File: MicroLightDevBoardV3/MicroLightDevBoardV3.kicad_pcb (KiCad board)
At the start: 2 copper layers, 12.9 x 18.9 mm, 26 parts, among them J1 TYPE-C-31-M-12, J2 Conn_01x02_Socket, J3 Conn_01x03_Socket, SW1 SW_Push, U1 USBLC6-2P6, U2 STM32C071GBUx, U3 BQ25180, U4 S-85S1AB33-I6T1U

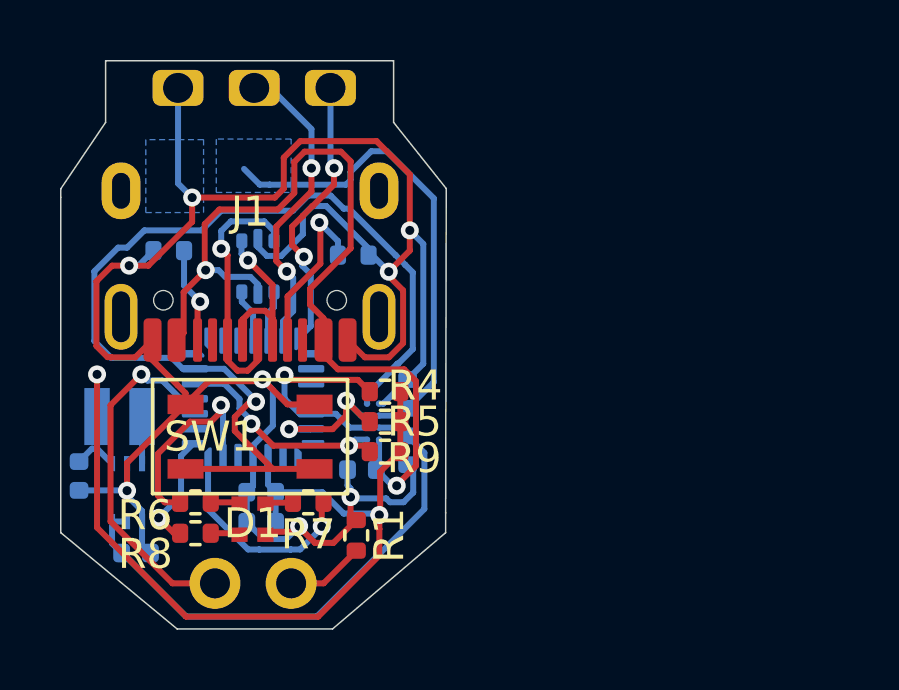
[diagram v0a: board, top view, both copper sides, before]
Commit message: change battery attachment from pad to through hole to increase durability
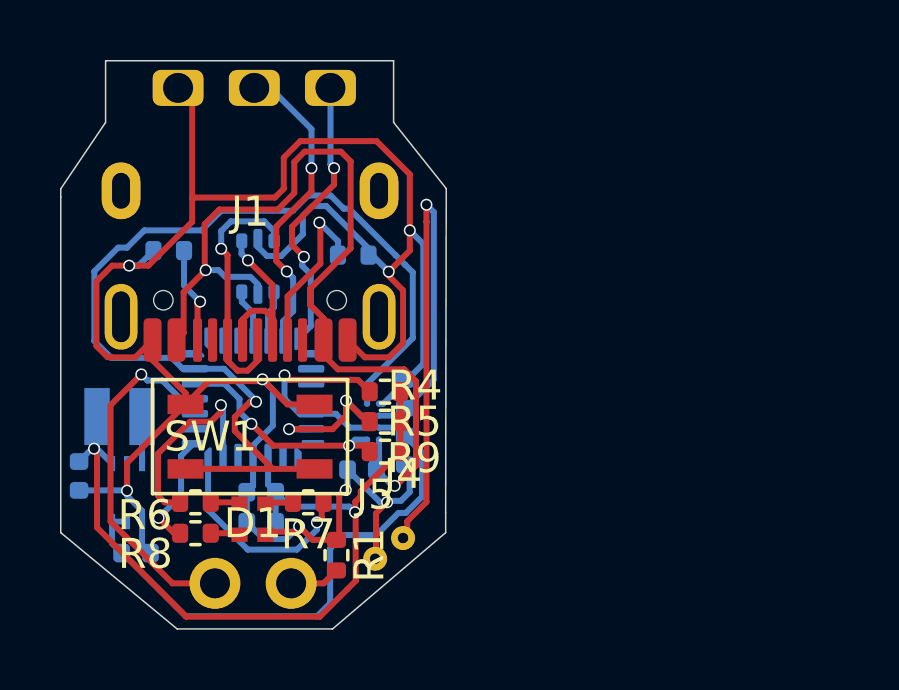
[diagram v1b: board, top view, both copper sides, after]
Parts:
- added J4: Conn_01x01_Socket, MicroLightDevBoard:battery_1x01_Vertical, F.Cu at (41.8, 33.2)
- added J5: Conn_01x01_Socket, MicroLightDevBoard:battery_1x01_Vertical, F.Cu at (40.9, 33.9)
- moved R1 0.93 mm to (39.6, 33.8)
- moved C5 0.08 mm to (41.9, 30.3)
- moved C6 0.08 mm to (41.9, 28.4)
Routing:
- net BAT_CHRG: track 16.2 -> 19.8 mm, vias 0 -> 1
- net +3.3V: track 32.4 -> 28.8 mm
- net GND: track 77.2 -> 79.6 mm
- net Net-(J2-Pin_2): track 2.62 -> 1.69 mm
- removed copper zone on B.Cu, net BAT_CHRG
- removed copper zone on B.Cu, net GND

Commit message: use 4 layer pcb and add accelerometer ic
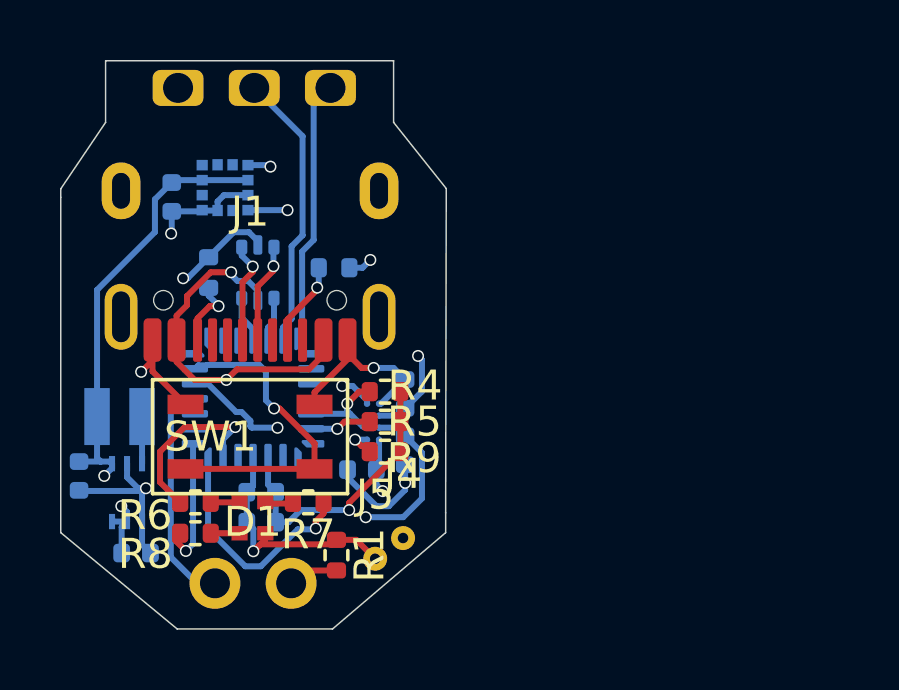
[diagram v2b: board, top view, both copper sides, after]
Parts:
- added C8: 100nF, Capacitor_SMD:C_0402_1005Metric, B.Cu at (34.1, 21.8)
- added U7: MC3479, Package_LGA:LGA-12_2x2mm_P0.5mm, B.Cu at (35.9, 21.5)
- moved R3 1.52 mm to (35.3, 24.3), turned to 90 degrees
- moved R2 0.77 mm to (39.5, 24.2)
- moved U1 0.21 mm to (37.0, 24.3)
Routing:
- net GND: track 79.6 -> 43.5 mm
- net TS_MR_CHRG: track 33.8 -> 14.6 mm, vias 1 -> 2
- net BAT_CHRG: track 19.8 -> 9.35 mm
- net I2C_SDA: track 5.32 -> 14.5 mm
- net VBUS_CHRG: track 29.5 -> 21.0 mm, vias 2 -> 3
- net I2C_SCL: track 6.99 -> 13.4 mm, vias 1 -> 2
- net Net-(J1-D+-PadA6): track 8.73 -> 3.32 mm
- net +3.3V: track 28.8 -> 32.9 mm
- net bulbLed: track 11.8 -> 7.70 mm, vias 1 -> 0
- net Net-(J1-D--PadA7): track 6.37 -> 3.39 mm
- net Net-(J1-CC1): track 5.73 -> 2.84 mm
- net SYS_CHRG: track 18.3 -> 16.7 mm, vias 0 -> 2
- net DEBUG_SWDIO: track 10.3 -> 9.36 mm, vias 2 -> 0
- net red: track 6.88 -> 5.98 mm
- net Net-(J1-CC2): track 3.24 -> 2.41 mm
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- added copper zone on In1.Cu, net GND
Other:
- copper layers 2 -> 4

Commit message: cleanup
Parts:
- moved R3 0.58 mm to (34.9, 24.0), turned to 180 degrees
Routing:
- net Net-(J1-D+-PadA6): track 3.32 -> 6.20 mm
- net Net-(J1-D--PadA7): track 3.39 -> 6.18 mm
- net I2C_SDA: track 14.5 -> 16.3 mm, vias 2 -> 3
- net red: track 5.98 -> 5.16 mm
- net INT_CHRG: track 7.39 -> 8.13 mm
- net GND: track 43.5 -> 43.9 mm, vias 8 -> 7

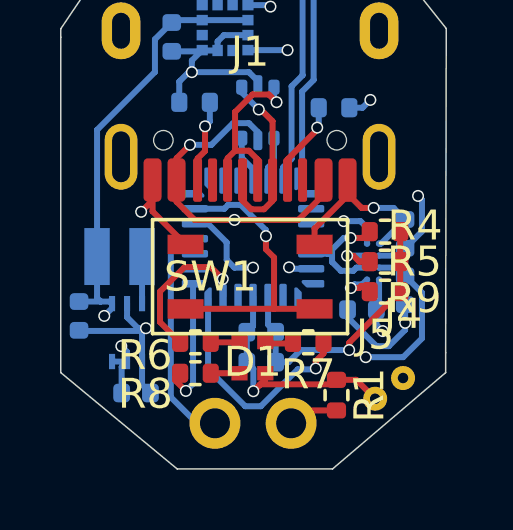
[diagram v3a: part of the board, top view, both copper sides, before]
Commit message: ground layer cleanup
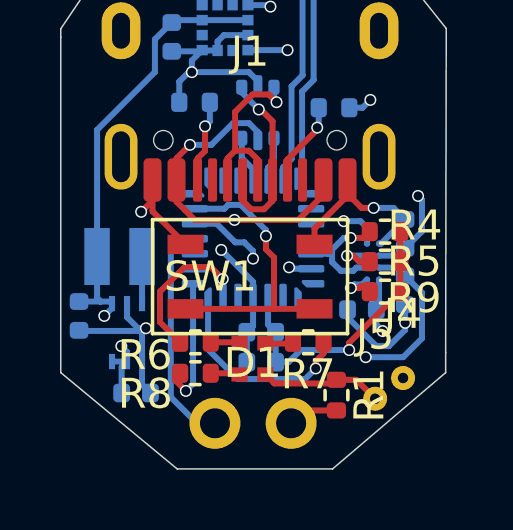
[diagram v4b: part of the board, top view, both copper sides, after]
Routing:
- net GND: track 43.9 -> 48.2 mm
- net green: track 7.95 -> 6.81 mm
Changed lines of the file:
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@@
 	(footprint "MicroLightDevBoard:RS-C1415MBAR"
 		(layer "F.Cu")
-		(at 36.78 32.5 90)
+		(at 36.78 32.54 90)
 		(property "Reference" "D1"
 			(at -0.14 0.01 0)
@@
 	)
 	(segment
-		(start 36.18 27.91)
-		(end 36.18 29.561479)
+		(start 40.996948 31.74)
+		(end 41.120459 31.616489)
 		(width 0.2)
 		(layer "In2.Cu")
@@
 	)
 	(segment
-		(start 36.18 29.561479)
-		(end 36.291 29.672479)
+		(start 36.291 28.021)
+		(end 36.291 30.021)
 		(width 0.2)
 		(layer "In2.Cu")
@@
 	)
 	(segment
-		(start 36.291 29.672479)
-		(end 36.291 30.021)
-		(width 0.2)
-		(layer "In2.Cu")
-		(net 1)
-	)
-	(segment
-		(start 40.996948 31.74)
-		(end 41.120459 31.616489)
+		(start 36.18 27.91)
+		(end 36.291 28.021)
 		(width 0.2)
 		(layer "In2.Cu")
@@
 	)
 	(segment
-		(start 37.21 33.22)
-		(end 37.21 33.07)
+		(start 39.459 33.361)
+		(end 37.511 33.361)
 		(width 0.2)
 		(layer "F.Cu")
@@
 	)
 	(segment
-		(start 36.81 33.62)
-		(end 37.039 33.391)
-		(width 0.2)
-		(layer "F.Cu")
-		(net 2)
-	)
-	(segment
-		(start 39.429 33.391)
-		(end 39.58 33.24)
+		(start 40.24 33.24)
+		(end 40.87 33.87)
 		(width 0.2)
 		(layer "F.Cu")
@@
 	)
 	(segment
-		(start 40.24 33.24)
-		(end 40.87 33.87)
+		(start 37.511 33.361)
+		(end 37.21 33.06)
 		(width 0.2)
 		(layer "F.Cu")
@@
 	)
 	(segment
-		(start 37.039 33.391)
-		(end 39.429 33.391)
+		(start 39.58 33.24)
+		(end 39.459 33.361)
 		(width 0.2)
 		(layer "F.Cu")
@@
 	)
 	(segment
-		(start 36.81 33.62)
-		(end 37.21 33.22)
-		(width 0.2)
-		(layer "F.Cu")
-		(net 2)
-	)
-	(segment
 		(start 39.58 33.24)
 		(end 40.24 33.24)
@@
 	)
 	(via
-		(at 33.07 27.64)
+		(at 35.74 28.91)
 		(size 0.4)
 		(drill 0.3)
@@
 	)
 	(via
-		(at 40.82 27.51)
+		(at 33.07 27.64)
 		(size 0.4)
 		(drill 0.3)
@@
 	)
 	(via
-		(at 36.81 33.62)
+		(at 40.82 27.51)
 		(size 0.4)
 		(drill 0.3)
 		(layers "F.Cu" "B.Cu")
-		(free yes)
 		(net 2)
 	)
@@
 	)
 	(segment
+		(start 36.8 29.97)
+		(end 35.74 28.91)
+		(width 0.2)
+		(layer "B.Cu")
+		(net 2)
+	)
+	(segment
 		(start 36.8 31.444882)
 		(end 36.592382 31.6525)
@@
 	)
 	(segment
-		(start 36.81 32.870118)
-		(end 36.592382 32.6525)
-		(width 0.2)
-		(layer "B.Cu")
-		(net 2)
-	)
-	(segment
 		(start 40.45 24.17)
 		(end 40.71 23.91)
@@
 	)
 	(segment
-		(start 36.81 33.62)
-		(end 36.81 32.870118)
-		(width 0.2)
-		(layer "B.Cu")
-		(net 2)
-	)
-	(segment
 		(start 32.6 30.7)
 		(end 32.6 31.154)
@@
 	)
 	(segment
+		(start 36.8 30.475)
+		(end 36.8 29.97)
+		(width 0.2)
+		(layer "B.Cu")
+		(net 2)
+	)
+	(segment
 		(start 34.34 23.3)
 		(end 34.34 23.99)
@@
 	)
 	(segment
-		(start 40.589 33.589)
-		(end 40.87 33.87)
-		(width 0.2)
-		(layer "In1.Cu")
-		(net 2)
-	)
-	(segment
-		(start 36.841 33.589)
-		(end 40.589 33.589)
+		(start 40.87 33.87)
+		(end 38.52 31.52)
 		(width 0.2)
 		(layer "In1.Cu")
@@
 	)
 	(segment
-		(start 36.81 33.62)
-		(end 36.841 33.589)
+		(start 40.87 33.189346)
+		(end 40.87 33.87)
 		(width 0.2)
 		(layer "In1.Cu")
@@
 	)
 	(segment
-		(start 40.87 33.189346)
-		(end 40.87 33.87)
+		(start 38.52 31.52)
+		(end 33.23 31.52)
 		(width 0.2)
 		(layer "In1.Cu")
@@
 	)
 	(segment
-		(start 38.86 32.89)
-		(end 38.29 32.89)
+		(start 38.5365 33.2135)
+		(end 38.89 32.86)
 		(width 0.2)
 		(layer "B.Cu")
@@
 	)
 	(segment
-		(start 35.3 32.88)
-		(end 35.3 30.535)
+		(start 35.3 30.535)
+		(end 35.3 32.226956)
 		(width 0.2)
 		(layer "B.Cu")
@@
 	)
 	(segment
-		(start 37.059 34.121)
-		(end 36.541 34.121)
+		(start 35.3 32.226956)
+		(end 36.286544 33.2135)
 		(width 0.2)
 		(layer "B.Cu")
@@
 	)
 	(segment
-		(start 38.89 32.86)
-		(end 38.86 32.89)
-		(width 0.2)
-		(layer "B.Cu")
-		(net 21)
-	)
-	(segment
-		(start 36.541 34.121)
-		(end 35.3 32.88)
-		(width 0.2)
-		(layer "B.Cu")
-		(net 21)
-	)
-	(segment
-		(start 38.29 32.89)
-		(end 37.059 34.121)
+		(start 36.286544 33.2135)
+		(end 38.5365 33.2135)
 		(width 0.2)
 		(layer "B.Cu")
@@
 	)
 	(via
-		(at 36.8 29.5)
+		(at 36.8 29.2)
 		(size 0.4)
 		(drill 0.3)
@@
 	)
 	(segment
-		(start 36.18 29.5)
-		(end 35.92 29.24)
+		(start 36.207501 28.657501)
+		(end 35.5875 28.0375)
 		(width 0.2)
 		(layer "B.Cu")
@@
 	)
 	(segment
-		(start 36.8 29.5)
-		(end 36.18 29.5)
+		(start 36.8 29.2)
+		(end 36.8 28.95)
 		(width 0.2)
 		(layer "B.Cu")
@@
 	)
 	(segment
-		(start 35.92 29.24)
-		(end 35.92 28.657501)
+		(start 35.5875 28.0375)
+		(end 34.8625 28.0375)
 		(width 0.2)
 		(layer "B.Cu")
@@
 	)
 	(segment
-		(start 35.92 28.657501)
-		(end 35.299999 28.0375)
+		(start 36.507501 28.657501)
+		(end 36.207501 28.657501)
 		(width 0.2)
 		(layer "B.Cu")
@@
 	)
 	(segment
-		(start 35.299999 28.0375)
-		(end 34.8625 28.0375)
+		(start 36.8 28.95)
+		(end 36.507501 28.657501)
 		(width 0.2)
 		(layer "B.Cu")
@@
 		(width 0.2)
 		(layer "In2.Cu")
+		(net 27)
+	)
+	(segment
+		(start 36.8 29.2)
+		(end 36.8 29.5)
+		(width 0.2)
+		(layer "In2.Cu")

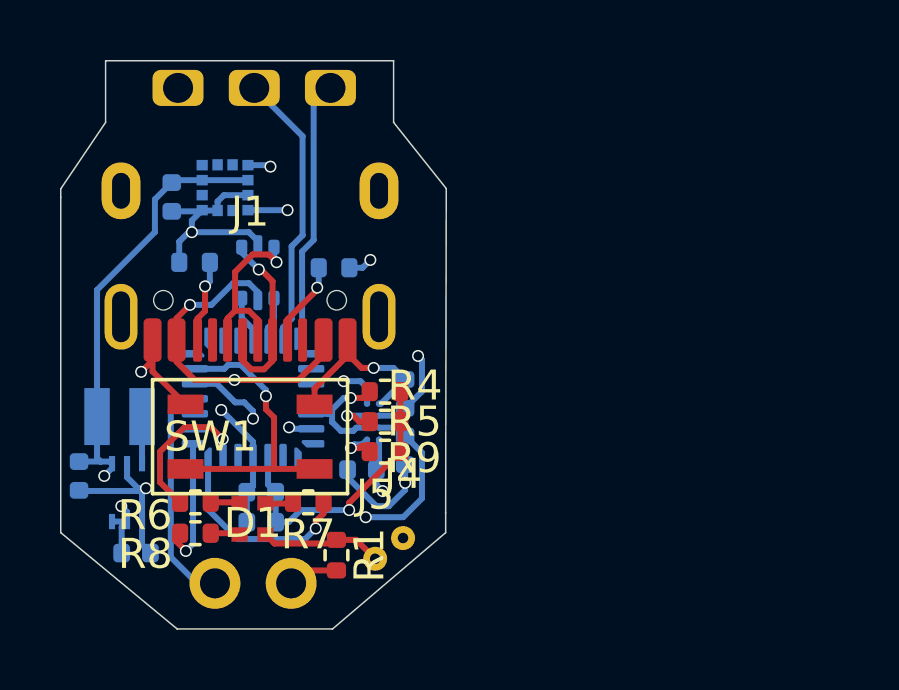
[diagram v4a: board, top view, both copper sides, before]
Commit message: 6 layer pcb design
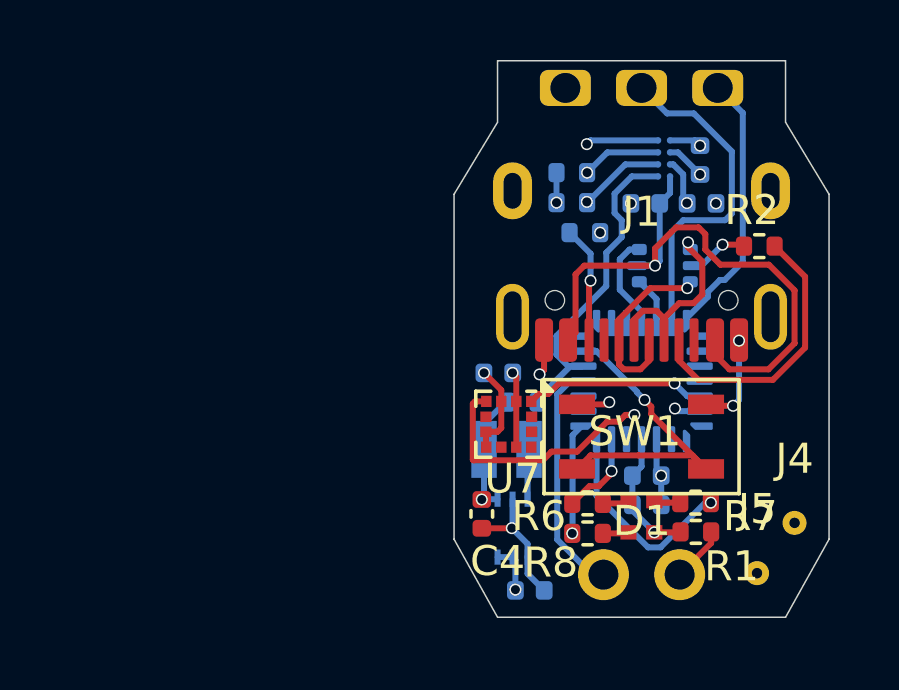
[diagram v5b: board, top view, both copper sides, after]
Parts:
- C4, R2, U7: moved to F.Cu
- R4, R5, R9: moved to B.Cu
- moved R2 14.2 mm to (53.7, 23.4), turned to 180 degrees
- moved U1 13.6 mm to (50.5, 24.1), turned to 180 degrees
- moved C4 13.5 mm to (44.4, 32.4)
- moved C7 13.2 mm to (46.0, 34.9)
- moved U3 13.1 mm to (50.5, 20.5)
- moved R6 13.1 mm to (48.0, 32.0)
- moved R8 13.1 mm to (48.0, 33.0)
- moved J4 13.1 mm to (54.9, 32.7)
- moved J1 13.0 mm to (49.8, 27.3)
- moved SW1 13.0 mm to (49.8, 29.8)
- moved R3 13.0 mm to (47.9, 23.0), turned to 0 degrees
- moved D1 13.0 mm to (49.7, 32.5)
- moved U2 13.0 mm to (49.8, 27.9)
- moved C3 13.0 mm to (49.9, 22.0)
- moved J2 13.0 mm to (48.5, 34.4)
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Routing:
- net +3.3V: track 32.9 -> 9.95 mm, vias 2 -> 4
- net GND: track 48.2 -> 30.7 mm, vias 7 -> 12
- net TS_MR_CHRG: track 14.6 -> 23.5 mm
- net Net-(J1-CC1): track 2.84 -> 9.40 mm, vias 1 -> 0
- net I2C_SDA: track 16.3 -> 22.8 mm
- net BAT_CHRG: track 9.35 -> 14.4 mm
- net INT_CHRG: track 8.12 -> 11.1 mm, vias 2 -> 0
- net SYS_CHRG: track 16.7 -> 19.5 mm
- net I2C_SCL: track 13.8 -> 16.5 mm
- net red: track 5.16 -> 2.86 mm
- net DEBUG_SWDIO: track 9.36 -> 11.3 mm
- net USB_DM: track 1.57 -> 3.21 mm
- net Net-(J1-CC2): track 2.76 -> 3.89 mm
- net blue: track 4.47 -> 3.70 mm
- net VBUS_CHRG: track 20.6 -> 21.0 mm, vias 3 -> 1
- added copper zone on In4.Cu, net +3.3V
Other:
- board size 12.9 x 18.9 mm -> 12.5 x 18.6 mm
- copper layers 4 -> 6

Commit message: add battery connector
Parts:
- added U5: DF53-2S-0.6H, MicroLightDevBoard:DF53-2S-0.6H, F.Cu at (54.1, 29.2)
- R1, R7: moved to B.Cu
- moved R1 4.74 mm to (47.0, 31.8), turned to 90 degrees
- moved J5 3.15 mm to (53.7, 31.2)
- moved J4 1.53 mm to (55.2, 31.2)
- moved R7 0.32 mm to (51.3, 32.2), turned to -90 degrees
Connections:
- J2 pad 1: bulbLed -> Net-(J2-Pin_1)
- J2 pad 2: Net-(J2-Pin_2) -> GND
- R1 pad 1: Net-(J2-Pin_2) -> Net-(J2-Pin_1)
- R1 pad 2: GND -> bulbLed
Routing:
- net bulbLed: track 7.93 -> 3.93 mm
- net Net-(J2-Pin_1): track 0.00 -> 3.46 mm
- net GND: track 30.7 -> 33.2 mm, vias 12 -> 13
- net Net-(J2-Pin_2): track 1.86 -> 0.00 mm
- net Net-(J1-CC1): track 9.40 -> 11.0 mm
- net green: track 6.97 -> 5.91 mm, vias 1 -> 0
- net BAT_CHRG: track 14.4 -> 13.9 mm, vias 1 -> 2
- net Net-(D1-GA): track 0.89 -> 1.23 mm, vias 0 -> 1
- added copper zone on In3.Cu, net +3.3V
- added copper zone on In4.Cu, net GND
- removed copper zone on In4.Cu, net +3.3V
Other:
- outline, holes or cut-outs redrawn

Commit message: cleanup
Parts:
- moved J5 3.13 mm to (53.5, 34.3)
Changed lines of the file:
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@@
 	(footprint "MicroLightDevBoard:battery_1x01_Vertical"
 		(layer "F.Cu")
-		(at 53.675 31.2)
+		(at 53.55 34.325)
 		(descr "Through hole straight socket strip, 1x01, 1.27mm pitch, single row (from Kicad 4.0.7), script generated")
 		(tags "Through hole socket strip THT 1x01 1.27mm single row")
@@
 			(type default)
 		)
+		(locked yes)
 		(layer "Edge.Cuts")
 	)
@@
 			(type default)
 		)
+		(locked yes)
 		(layer "Edge.Cuts")
 	)
@@
 			(type default)
 		)
+		(locked yes)
 		(layer "Edge.Cuts")
 	)
@@
 			(type default)
 		)
+		(locked yes)
 		(layer "Edge.Cuts")
 	)
@@
 	)
 	(segment
-		(start 49.6 28.300001)
-		(end 48.249999 26.95)
+		(start 48.249999 26.95)
+		(end 49.85 28.550001)
 		(width 0.2)
 		(layer "B.Cu")
@@
 	)
 	(segment
-		(start 49.6 28.325)
-		(end 49.6 28.300001)
-		(width 0.2)
-		(layer "B.Cu")
-		(net 19)
-	)
-	(segment
 		(start 48.049998 19.925002)
 		(end 50.3 19.925002)
@@
 	)
 	(segment
-		(start 48.249999 26.95)
-		(end 47.8125 26.95)
+		(start 47.8125 26.95)
+		(end 48.249999 26.95)
 		(width 0.2)
 		(layer "B.Cu")
@@
 	)
 	(segment
-		(start 49.85 28.575)
-		(end 49.6 28.325)
+		(start 49.85 28.550001)
+		(end 49.85 28.575)
 		(width 0.2)
 		(layer "B.Cu")

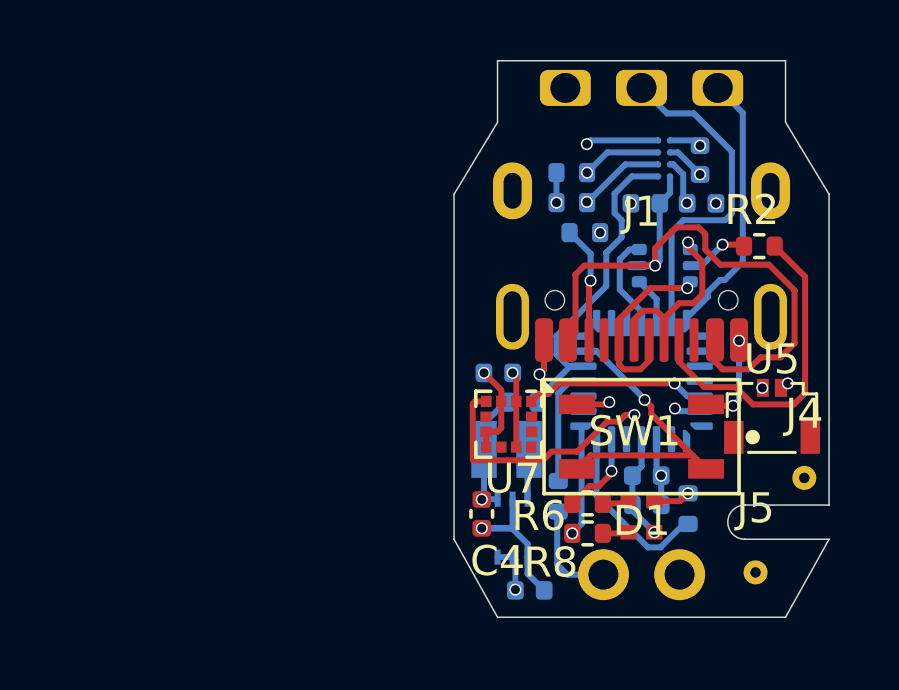
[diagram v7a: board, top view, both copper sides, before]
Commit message: lcsc ids, adjust footprints, cleanup
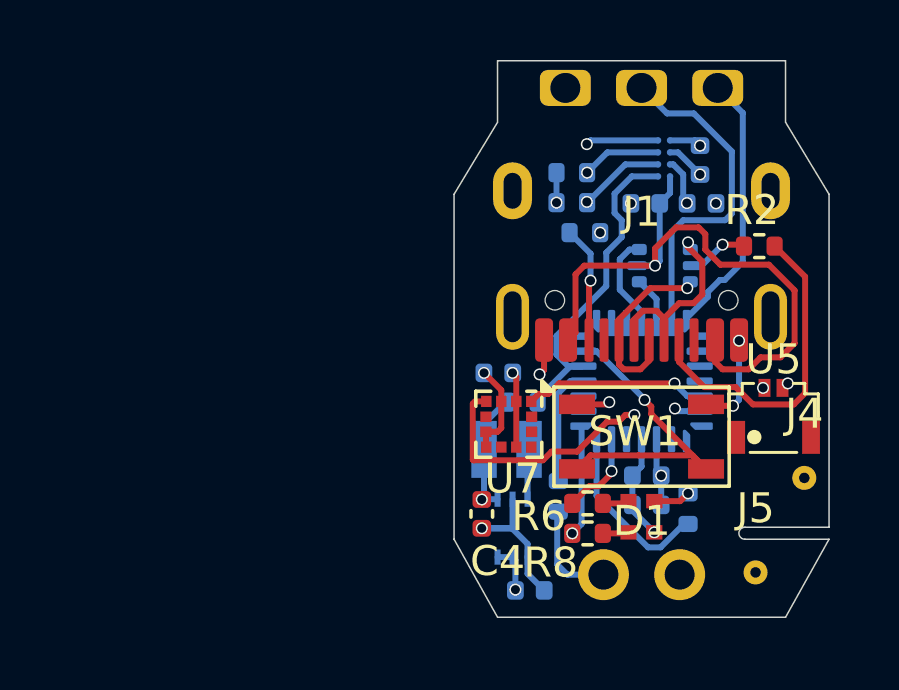
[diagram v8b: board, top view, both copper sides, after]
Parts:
- moved U5 0.05 mm to (54.1, 29.2)
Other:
- outline, holes or cut-outs redrawn
